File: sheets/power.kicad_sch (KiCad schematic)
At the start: 81 parts, among them J4 POWER JACK, Q11 C1815, Q12 A1015, Q13 A1442, SW2 POWER SWITCH, T1 SH-302, U11 74LS05, U12 74LS06, U28 PC4741, U29 PC4741, U33 74AS04, U37 LM2576T-5, U38 74HC32, U8 74HC04, U80 74HC04

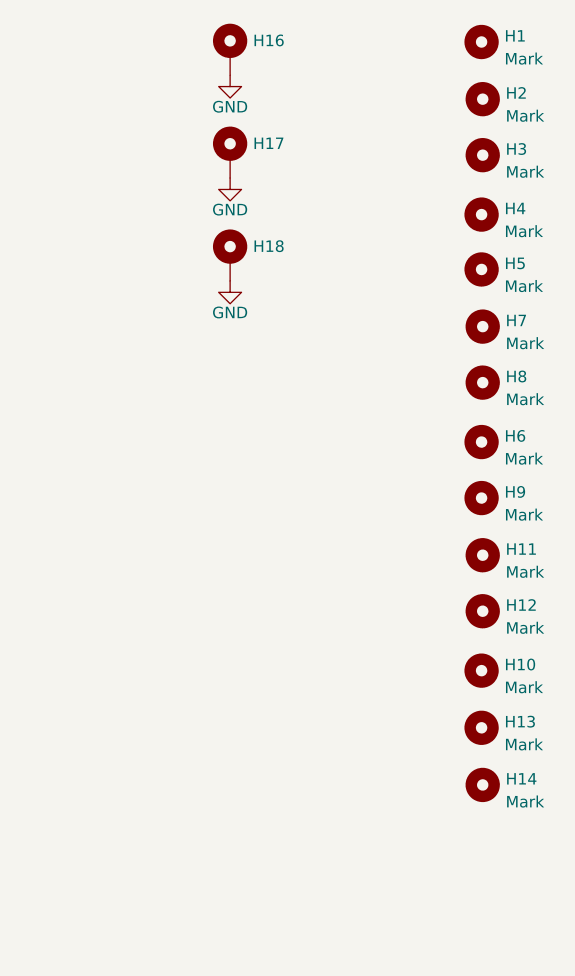
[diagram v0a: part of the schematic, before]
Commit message: Increase size of Diode Project Tidy up
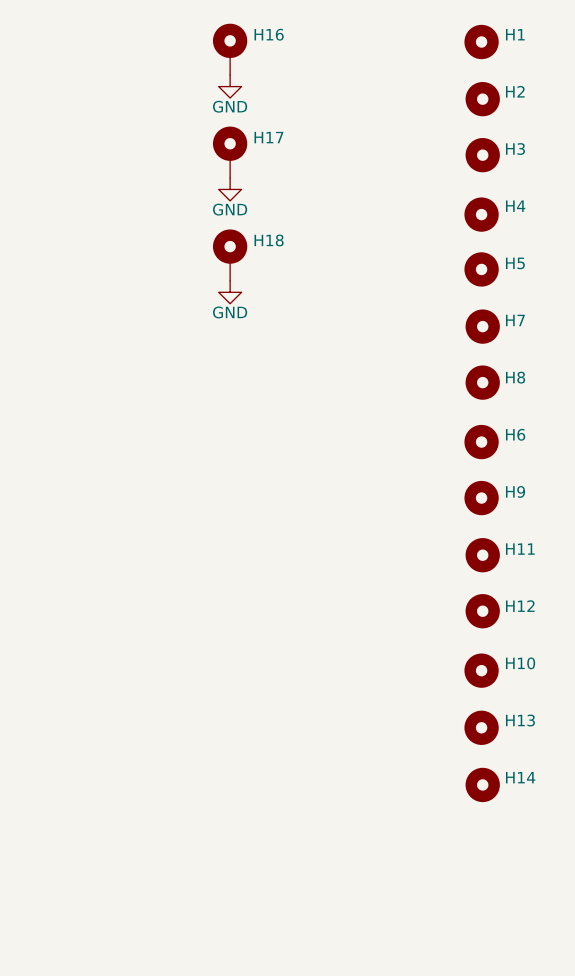
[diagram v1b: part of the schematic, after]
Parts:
- H1, H10, H11, H12, H13, H14, H2, H3, H4, H5, H6, H7, H8, H9: value Mark -> ~
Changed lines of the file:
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@@
   )
   (symbol (lib_id "Mechanical:MountingHole_Pad") (at 368.3 41.275 0) (unit 1)
-    (in_bom yes) (on_board yes) (dnp no) (fields_autoplaced)
-    (property "Reference" "H18" (at 370.84 40.005 0)
+    (in_bom yes) (on_board yes) (dnp no)
+    (property "Reference" "H18" (at 370.84 39.37 0)
       (effects (font (size 1.27 1.27)) (justify left))
     )
@@
   )
   (symbol (lib_id "1_NeoGeoLibrary:MARK") (at 396.24 93.472 0) (unit 1)
-    (in_bom yes) (on_board yes) (dnp no) (fields_autoplaced)
-    (property "Reference" "H13" (at 398.78 92.837 0)
-      (effects (font (size 1.27 1.27)) (justify left))
-    )
-    (property "Value" "Mark" (at 398.78 95.377 0)
+    (in_bom yes) (on_board yes) (dnp no)
+    (property "Reference" "H13" (at 398.78 92.71 0)
+      (effects (font (size 1.27 1.27)) (justify left))
+    )
+    (property "Value" "~" (at 398.78 95.377 0)
       (effects (font (size 1.27 1.27)) (justify left))
     )
@@
   )
   (symbol (lib_id "1_NeoGeoLibrary:MARK") (at 396.24 17.272 0) (unit 1)
-    (in_bom yes) (on_board yes) (dnp no) (fields_autoplaced)
-    (property "Reference" "H1" (at 398.78 16.637 0)
-      (effects (font (size 1.27 1.27)) (justify left))
-    )
-    (property "Value" "Mark" (at 398.78 19.177 0)
+    (in_bom yes) (on_board yes) (dnp no)
+    (property "Reference" "H1" (at 398.78 16.51 0)
+      (effects (font (size 1.27 1.27)) (justify left))
+    )
+    (property "Value" "~" (at 398.78 19.177 0)
       (effects (font (size 1.27 1.27)) (justify left))
     )
@@
   )
   (symbol (lib_id "1_NeoGeoLibrary:MARK") (at 396.24 61.722 0) (unit 1)
-    (in_bom yes) (on_board yes) (dnp no) (fields_autoplaced)
-    (property "Reference" "H6" (at 398.78 61.087 0)
-      (effects (font (size 1.27 1.27)) (justify left))
-    )
-    (property "Value" "Mark" (at 398.78 63.627 0)
+    (in_bom yes) (on_board yes) (dnp no)
+    (property "Reference" "H6" (at 398.78 60.96 0)
+      (effects (font (size 1.27 1.27)) (justify left))
+    )
+    (property "Value" "~" (at 398.78 63.627 0)
       (effects (font (size 1.27 1.27)) (justify left))
     )
@@
   )
   (symbol (lib_id "1_NeoGeoLibrary:MARK") (at 396.367 29.845 0) (unit 1)
-    (in_bom yes) (on_board yes) (dnp no) (fields_autoplaced)
-    (property "Reference" "H3" (at 398.907 29.21 0)
-      (effects (font (size 1.27 1.27)) (justify left))
-    )
-    (property "Value" "Mark" (at 398.907 31.75 0)
+    (in_bom yes) (on_board yes) (dnp no)
+    (property "Reference" "H3" (at 398.78 29.21 0)
+      (effects (font (size 1.27 1.27)) (justify left))
+    )
+    (property "Value" "~" (at 398.907 31.75 0)
       (effects (font (size 1.27 1.27)) (justify left))
     )
@@
   )
   (symbol (lib_id "1_NeoGeoLibrary:MARK") (at 396.367 99.822 0) (unit 1)
-    (in_bom yes) (on_board yes) (dnp no) (fields_autoplaced)
-    (property "Reference" "H14" (at 398.907 99.187 0)
-      (effects (font (size 1.27 1.27)) (justify left))
-    )
-    (property "Value" "Mark" (at 398.907 101.727 0)
+    (in_bom yes) (on_board yes) (dnp no)
+    (property "Reference" "H14" (at 398.78 99.06 0)
+      (effects (font (size 1.27 1.27)) (justify left))
+    )
+    (property "Value" "~" (at 398.907 101.727 0)
       (effects (font (size 1.27 1.27)) (justify left))
     )
@@
   )
   (symbol (lib_id "1_NeoGeoLibrary:MARK") (at 396.24 42.545 0) (unit 1)
-    (in_bom yes) (on_board yes) (dnp no) (fields_autoplaced)
+    (in_bom yes) (on_board yes) (dnp no)
     (property "Reference" "H5" (at 398.78 41.91 0)
       (effects (font (size 1.27 1.27)) (justify left))
     )
-    (property "Value" "Mark" (at 398.78 44.45 0)
+    (property "Value" "~" (at 398.78 44.45 0)
       (effects (font (size 1.27 1.27)) (justify left))
     )
@@
   )
   (symbol (lib_id "1_NeoGeoLibrary:MARK") (at 396.367 80.518 0) (unit 1)
-    (in_bom yes) (on_board yes) (dnp no) (fields_autoplaced)
-    (property "Reference" "H12" (at 398.907 79.883 0)
-      (effects (font (size 1.27 1.27)) (justify left))
-    )
-    (property "Value" "Mark" (at 398.907 82.423 0)
+    (in_bom yes) (on_board yes) (dnp no)
+    (property "Reference" "H12" (at 398.78 80.01 0)
+      (effects (font (size 1.27 1.27)) (justify left))
+    )
+    (property "Value" "~" (at 398.907 82.423 0)
       (effects (font (size 1.27 1.27)) (justify left))
     )
@@
   )
   (symbol (lib_id "1_NeoGeoLibrary:MARK") (at 396.367 55.118 0) (unit 1)
-    (in_bom yes) (on_board yes) (dnp no) (fields_autoplaced)
-    (property "Reference" "H8" (at 398.907 54.483 0)
-      (effects (font (size 1.27 1.27)) (justify left))
-    )
-    (property "Value" "Mark" (at 398.907 57.023 0)
+    (in_bom yes) (on_board yes) (dnp no)
+    (property "Reference" "H8" (at 398.78 54.61 0)
+      (effects (font (size 1.27 1.27)) (justify left))
+    )
+    (property "Value" "~" (at 398.907 57.023 0)
       (effects (font (size 1.27 1.27)) (justify left))
     )
@@
   )
   (symbol (lib_id "1_NeoGeoLibrary:MARK") (at 396.24 87.122 0) (unit 1)
-    (in_bom yes) (on_board yes) (dnp no) (fields_autoplaced)
-    (property "Reference" "H10" (at 398.78 86.487 0)
-      (effects (font (size 1.27 1.27)) (justify left))
-    )
-    (property "Value" "Mark" (at 398.78 89.027 0)
+    (in_bom yes) (on_board yes) (dnp no)
+    (property "Reference" "H10" (at 398.78 86.36 0)
+      (effects (font (size 1.27 1.27)) (justify left))
+    )
+    (property "Value" "~" (at 398.78 89.027 0)
       (effects (font (size 1.27 1.27)) (justify left))
     )
@@
   )
   (symbol (lib_id "1_NeoGeoLibrary:MARK") (at 396.24 67.945 0) (unit 1)
-    (in_bom yes) (on_board yes) (dnp no) (fields_autoplaced)
+    (in_bom yes) (on_board yes) (dnp no)
     (property "Reference" "H9" (at 398.78 67.31 0)
       (effects (font (size 1.27 1.27)) (justify left))
     )
-    (property "Value" "Mark" (at 398.78 69.85 0)
+    (property "Value" "~" (at 398.78 69.85 0)
       (effects (font (size 1.27 1.27)) (justify left))
     )
@@
   )
   (symbol (lib_id "Mechanical:MountingHole_Pad") (at 368.3 18.415 0) (unit 1)
-    (in_bom yes) (on_board yes) (dnp no) (fields_autoplaced)
-    (property "Reference" "H16" (at 370.84 17.145 0)
+    (in_bom yes) (on_board yes) (dnp no)
+    (property "Reference" "H16" (at 370.84 16.51 0)
       (effects (font (size 1.27 1.27)) (justify left))
     )
@@
   )
   (symbol (lib_id "Mechanical:MountingHole_Pad") (at 368.3 29.845 0) (unit 1)
-    (in_bom yes) (on_board yes) (dnp no) (fields_autoplaced)
-    (property "Reference" "H17" (at 370.84 28.575 0)
+    (in_bom yes) (on_board yes) (dnp no)
+    (property "Reference" "H17" (at 370.84 27.94 0)
       (effects (font (size 1.27 1.27)) (justify left))
     )
@@
   )
   (symbol (lib_id "1_NeoGeoLibrary:MARK") (at 396.367 48.895 0) (unit 1)
-    (in_bom yes) (on_board yes) (dnp no) (fields_autoplaced)
-    (property "Reference" "H7" (at 398.907 48.26 0)
-      (effects (font (size 1.27 1.27)) (justify left))
-    )
-    (property "Value" "Mark" (at 398.907 50.8 0)
+    (in_bom yes) (on_board yes) (dnp no)
+    (property "Reference" "H7" (at 398.78 48.26 0)
+      (effects (font (size 1.27 1.27)) (justify left))
+    )
+    (property "Value" "~" (at 398.907 50.8 0)
       (effects (font (size 1.27 1.27)) (justify left))
     )
@@
   )
   (symbol (lib_id "1_NeoGeoLibrary:MARK") (at 396.367 74.295 0) (unit 1)
-    (in_bom yes) (on_board yes) (dnp no) (fields_autoplaced)
-    (property "Reference" "H11" (at 398.907 73.66 0)
-      (effects (font (size 1.27 1.27)) (justify left))
-    )
-    (property "Value" "Mark" (at 398.907 76.2 0)
+    (in_bom yes) (on_board yes) (dnp no)
+    (property "Reference" "H11" (at 398.78 73.66 0)
+      (effects (font (size 1.27 1.27)) (justify left))
+    )
+    (property "Value" "~" (at 398.907 76.2 0)
       (effects (font (size 1.27 1.27)) (justify left))
     )
@@
   )
   (symbol (lib_id "1_NeoGeoLibrary:MARK") (at 396.24 36.449 0) (unit 1)
-    (in_bom yes) (on_board yes) (dnp no) (fields_autoplaced)
-    (property "Reference" "H4" (at 398.78 35.814 0)
-      (effects (font (size 1.27 1.27)) (justify left))
-    )
-    (property "Value" "Mark" (at 398.78 38.354 0)
+    (in_bom yes) (on_board yes) (dnp no)
+    (property "Reference" "H4" (at 398.78 35.56 0)
+      (effects (font (size 1.27 1.27)) (justify left))
+    )
+    (property "Value" "~" (at 398.78 38.354 0)
       (effects (font (size 1.27 1.27)) (justify left))
     )
@@
   )
   (symbol (lib_id "1_NeoGeoLibrary:MARK") (at 396.367 23.622 0) (unit 1)
-    (in_bom yes) (on_board yes) (dnp no) (fields_autoplaced)
-    (property "Reference" "H2" (at 398.907 22.987 0)
-      (effects (font (size 1.27 1.27)) (justify left))
-    )
-    (property "Value" "Mark" (at 398.907 25.527 0)
-      (effects (font (size 1.27 1.27)) (justify left))
-    )
+    (in_bom yes) (on_board yes) (dnp no)
+    (property "Reference" "H2" (at 398.78 22.86 0)
+      (effects (font (size 1.27 1.27)) (justify left))
+    )
+    (property "Value" "~" (at 398.907 25.527 0)
+      (effects (font (size 1.27 1.27)) (justify left))
+    )

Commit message: More little tweaks
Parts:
- D1, D2, L3, U37: Comment (none) -> Not Fitted when 5v Circuit
- D11, D12, D13, Q11, Q12, Q13, R76, R77, R78, R79, R80, R81, R82, R83: Comment (none) -> Not Fitted when 9v Circuit
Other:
- note added: "5v Circuit Not Fitted"
- note added: "9v Circuit"
- note added: "Not Fitted 5v overprotection circuit If board is configured for 5v PSU and not 9V which uses the LM2576T"
- note removed: "Not Fitted"
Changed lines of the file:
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@@
   (junction (at 201.295 127) (diameter 0) (color 0 0 0 0)
   )
-  (junction (at 62.484 65.786) (diameter 0) (color 0 0 0 0)
-  )
   (junction (at 211.455 132.08) (diameter 0) (color 0 0 0 0)
   )
@@
   (junction (at 133.858 60.706) (diameter 0) (color 0 0 0 0)
   )
+  (junction (at 65.278 65.786) (diameter 0) (color 0 0 0 0)
+  )
   (junction (at 152.146 246.38) (diameter 0) (color 0 0 0 0)
   )
@@
     (stroke (width 0) (type default))
   )
-  (wire (pts (xy 51.562 65.786) (xy 62.484 65.786))
-    (stroke (width 0) (type default))
-  )
   (wire (pts (xy 150.495 132.08) (xy 160.655 132.08))
     (stroke (width 0) (type default))
@@
     (stroke (width 0) (type default))
   )
-  (wire (pts (xy 62.484 60.706) (xy 120.904 60.706))
+  (wire (pts (xy 65.278 60.706) (xy 120.904 60.706))
     (stroke (width 0) (type default))
   )
@@
     (stroke (width 0) (type default))
   )
-  (wire (pts (xy 72.39 74.93) (xy 62.484 74.93))
+  (wire (pts (xy 72.39 74.93) (xy 65.278 74.93))
     (stroke (width 0) (type default))
   )
@@
     (stroke (width 0) (type default))
   )
-  (wire (pts (xy 67.056 65.786) (xy 62.484 65.786))
+  (wire (pts (xy 67.056 65.786) (xy 65.278 65.786))
     (stroke (width 0) (type default))
   )
@@
     (stroke (width 0) (type default))
   )
+  (wire (pts (xy 51.562 65.786) (xy 65.278 65.786))
+    (stroke (width 0) (type default))
+  )
   (wire (pts (xy 95.504 65.786) (xy 95.504 69.85))
     (stroke (width 0) (type default))
@@
     (stroke (width 0) (type default))
   )
-  (wire (pts (xy 62.484 65.786) (xy 62.484 60.706))
+  (wire (pts (xy 65.278 65.786) (xy 65.278 60.706))
     (stroke (width 0) (type default))
   )
@@
     (stroke (width 0) (type default))
   )
-  (wire (pts (xy 62.484 74.93) (xy 62.484 65.786))
+  (wire (pts (xy 65.278 74.93) (xy 65.278 65.786))
     (stroke (width 0) (type default))
   )
@@
     (fill (type none))
   )
-  (text "Not Fitted" (at 43.942 64.135 0)
+  (rectangle (start 120.396 47.498) (end 269.494 84.074)
+    (stroke (width 0) (type dash))
+    (fill (type none))
+  )
+  (text "Not Fitted 5v overprotection circuit\nIf board is configured for 5v PSU and not 9V\nwhich uses the LM2576T"
+    (at 44.196 113.538 0)
+    (effects (font (size 1.27 1.27)) (justify left bottom))
+  )
+  (text "5v Circuit Not Fitted" (at 44.196 64.77 0)
     (effects (font (size 1.27 1.27)) (justify left bottom))
   )
@@
     (effects (font (size 1.27 1.27)) (justify left bottom))
   )
+  (text "9v Circuit" (at 120.904 50.038 0)
+    (effects (font (size 1.27 1.27)) (justify left bottom))
+  )
   (text "N.F" (at 98.552 78.994 0)
     (effects (font (size 1.27 1.27)) (justify left bottom))
@@
       (effects (font (size 1.27 1.27)) hide)
     )
+    (property "Comment" "Not Fitted when 5v Circuit" (at 187.833 63.246 0)
+      (effects (font (size 1.27 1.27)) hide)
+    )
     (pin "1")
     (pin "2")
@@
       (effects (font (size 1.27 1.27)) hide)
     )
+    (property "Comment" "Not Fitted when 9v Circuit" (at 92.964 74.93 0)
+      (effects (font (size 1.27 1.27)) hide)
+    )
     (pin "1")
     (pin "2")
@@
       (effects (font (size 1.27 1.27)) hide)
     )
+    (property "Comment" "Not Fitted when 9v Circuit" (at 108.966 74.676 0)
+      (effects (font (size 1.27 1.27)) hide)
+    )
     (pin "1")
     (pin "2")
@@
       (effects (font (size 1.27 1.27)) hide)
     )
+    (property "Comment" "Not Fitted when 9v Circuit" (at 108.966 104.14 0)
+      (effects (font (size 1.27 1.27)) hide)
+    )
     (pin "1")
     (pin "2")
@@
       (effects (font (size 1.27 1.27)) (justify left) hide)
     )
+    (property "Comment" "Not Fitted when 9v Circuit" (at 77.47 77.47 0)
+      (effects (font (size 1.27 1.27)) hide)
+    )
     (pin "1")
     (pin "2")
@@
       (effects (font (size 1.27 1.27)) hide)
     )
+    (property "Comment" "Not Fitted when 9v Circuit" (at 49.276 80.137 0)
+      (effects (font (size 1.27 1.27)) hide)
+    )
     (pin "1")
     (pin "2")
@@
       (effects (font (size 1.27 1.27)) hide)
     )
+    (property "Comment" "Not Fitted when 9v Circuit" (at 85.09 77.724 0)
+      (effects (font (size 1.27 1.27)) hide)
+    )
     (pin "1")
     (pin "2")
@@
       (effects (font (size 1.27 1.27)) (justify left) hide)
     )
+    (property "Comment" "Not Fitted when 9v Circuit" (at 56.642 89.154 0)
+      (effects (font (size 1.27 1.27)) hide)
+    )
     (pin "1")
     (pin "2")
@@
       (effects (font (size 1.27 1.27)) hide)
     )
+    (property "Comment" "" (at 140.589 68.326 0)
+      (effects (font (size 1.27 1.27)) hide)
+    )
     (pin "1")
     (pin "2")
@@
   (symbol (lib_id "1_NeoGeoLibrary:SW_Push_SPDT") (at 37.846 65.786 0) (mirror y) (unit 1)
     (in_bom yes) (on_board yes) (dnp no)
-    (property "Reference" "SW2" (at 37.846 61.722 0)
+    (property "Reference" "SW2" (at 36.068 60.96 0)
       (effects (font (size 1.27 1.27)))
     )
-    (property "Value" "POWER SWITCH" (at 34.29 71.12 0)
+    (property "Value" "POWER SWITCH" (at 25.908 66.04 0)
       (effects (font (size 1.27 1.27)))
     )
@@
       (effects (font (size 1.27 1.27)) hide)
     )
+    (property "Comment" "Not Fitted when 9v Circuit" (at 51.562 80.137 0)
+      (effects (font (size 1.27 1.27)) hide)
+    )
     (pin "1")
     (pin "2")
@@
       (effects (font (size 1.27 1.27)) hide)
     )
+    (property "Comment" "Not Fitted when 9v Circuit" (at 69.596 65.786 0)
+      (effects (font (size 1.27 1.27)) hide)
+    )
     (pin "1")
     (pin "2")
@@
       (effects (font (size 1.27 1.27)) hide)
     )
+    (property "Comment" "Not Fitted when 5v Circuit" (at 212.852 70.866 0)
+      (effects (font (size 1.27 1.27)) hide)
+    )
     (pin "1")
     (pin "2")
@@
       (effects (font (size 1.27 1.27)) hide)
     )
+    (property "Comment" "Not Fitted when 5v Circuit" (at 124.714 60.706 0)
+      (effects (font (size 1.27 1.27)) hide)
+    )
     (pin "1")
     (pin "2")
@@
       (effects (font (size 1.27 1.27)) hide)
     )
+    (property "Comment" "Not Fitted when 9v Circuit" (at 180.34 111.125 0)
+      (effects (font (size 1.27 1.27)) hide)
+    )
     (pin "1")
     (pin "2")
@@
       (effects (font (size 1.27 1.27)) hide)
     )
+    (property "Comment" "Not Fitted when 9v Circuit" (at 68.58 86.614 0)
+      (effects (font (size 1.27 1.27)) hide)
+    )
     (pin "1")
     (pin "2")
@@
       (effects (font (size 1.27 1.27)) hide)
     )
+    (property "Comment" "Not Fitted when 9v Circuit" (at 108.966 91.059 0)
+      (effects (font (size 1.27 1.27)) hide)
+    )
     (pin "1")
     (pin "2")
@@
       (effects (font (size 1.27 1.27)))
     )
+    (property "Comment" "Not Fitted when 5v Circuit" (at 236.093 65.786 0)
+      (effects (font (size 1.27 1.27)) hide)
+    )
     (pin "1")
     (pin "2")
@@
       (effects (font (size 1.27 1.27)) hide)
     )
+    (property "Comment" "Not Fitted when 9v Circuit" (at 51.562 69.596 0)
+      (effects (font (size 1.27 1.27)) hide)
+    )
     (pin "1")
     (pin "2")
@@
       (effects (font (size 1.27 1.27)) hide)
     )
+    (property "Comment" "Not Fitted when 9v Circuit" (at 108.966 97.536 0)
+      (effects (font (size 1.27 1.27)) hide)
+    )

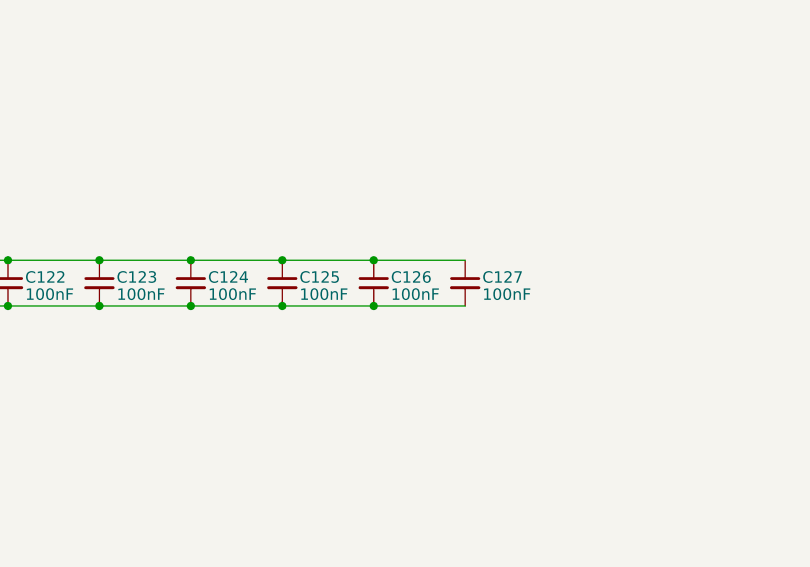
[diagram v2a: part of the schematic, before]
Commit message: Adding Mouser Part Numbers
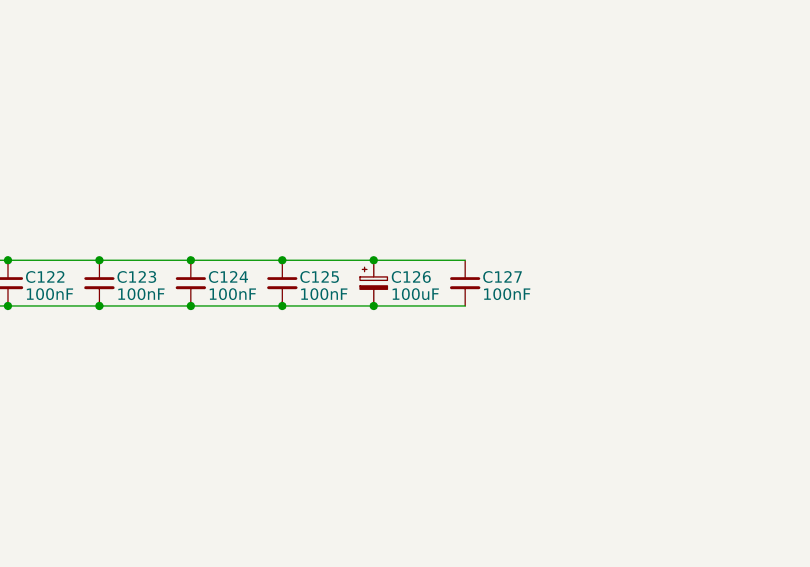
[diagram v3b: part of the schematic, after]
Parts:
- C101, C102, C103, C104, C105, C106, C107, C108, C109, C110, C111, C112, C114, C115, C116, C117, C118, C119, C120, C121, C122, C123, C124, C125, C127: Mouser (none) -> 810-FG26C0G1H104JNT0
- C113: Mouser (none) -> 667-ECA-1CM100I
- C126: value 100nF -> 100uF; symbol Device:C_Small -> Device:C_Polarized_Small; Mouser (none) -> 667-ECA-1CM101I
- C201: Mouser (none) -> 810-FG28C0G1H101JNT6
- C44, C45: Mouser (none) -> 810-FG28C0G1H103JNT0
- C47: Mouser (none) -> 667-EEU-FC0J222S
